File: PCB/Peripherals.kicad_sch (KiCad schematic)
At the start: 25 parts, among them J1 104031-0811, J3 BM04B-GHS-TBT, J4 BM06B-GHS-TBT, J5 BDL-108-X-X, J6 BM06B-GHS-TBT, J7 BM04B-GHS-TBT, U3 FM25V02A-GTR

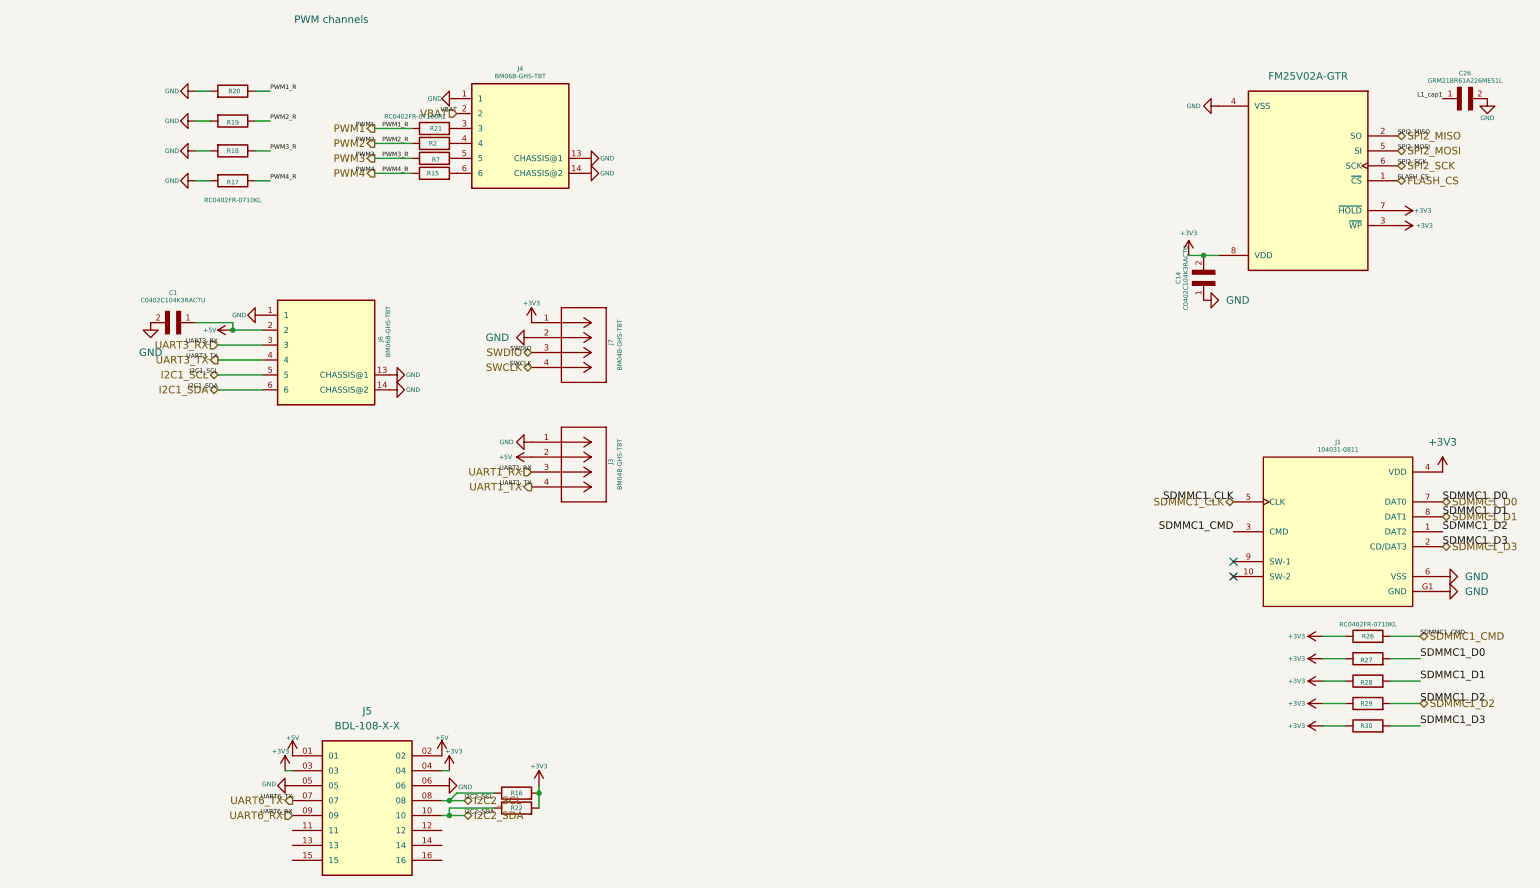
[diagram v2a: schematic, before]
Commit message: Peripherals: replace JST-GH/Samtec with castellated pad-row connectors
- Deleted J3/J4/J5/J6/J7 (JST-GH + Samtec)
- Added J3 GPS(PADROW-6), J4 TELEM(PADROW-5), J5 I2C2(PADROW-4),
  J6 SPI2(PADROW-6), J7 SWD(PADROW-5), J8 GPIO-EXP(HEADER-2x6),
  J9 MOTOR(PADROW-4), J10 BUZZ(PADROW-2), J11 LED(PADROW-2)
- Connected all pads to nets via Konnect connect_to_net
- NOTE: PWM series-resistor network (R2/R7/R15/R21) now orphaned, needs rebuild
- New nets needing root connection: GPIO_A0..A7, BUZZ, LED, NRST
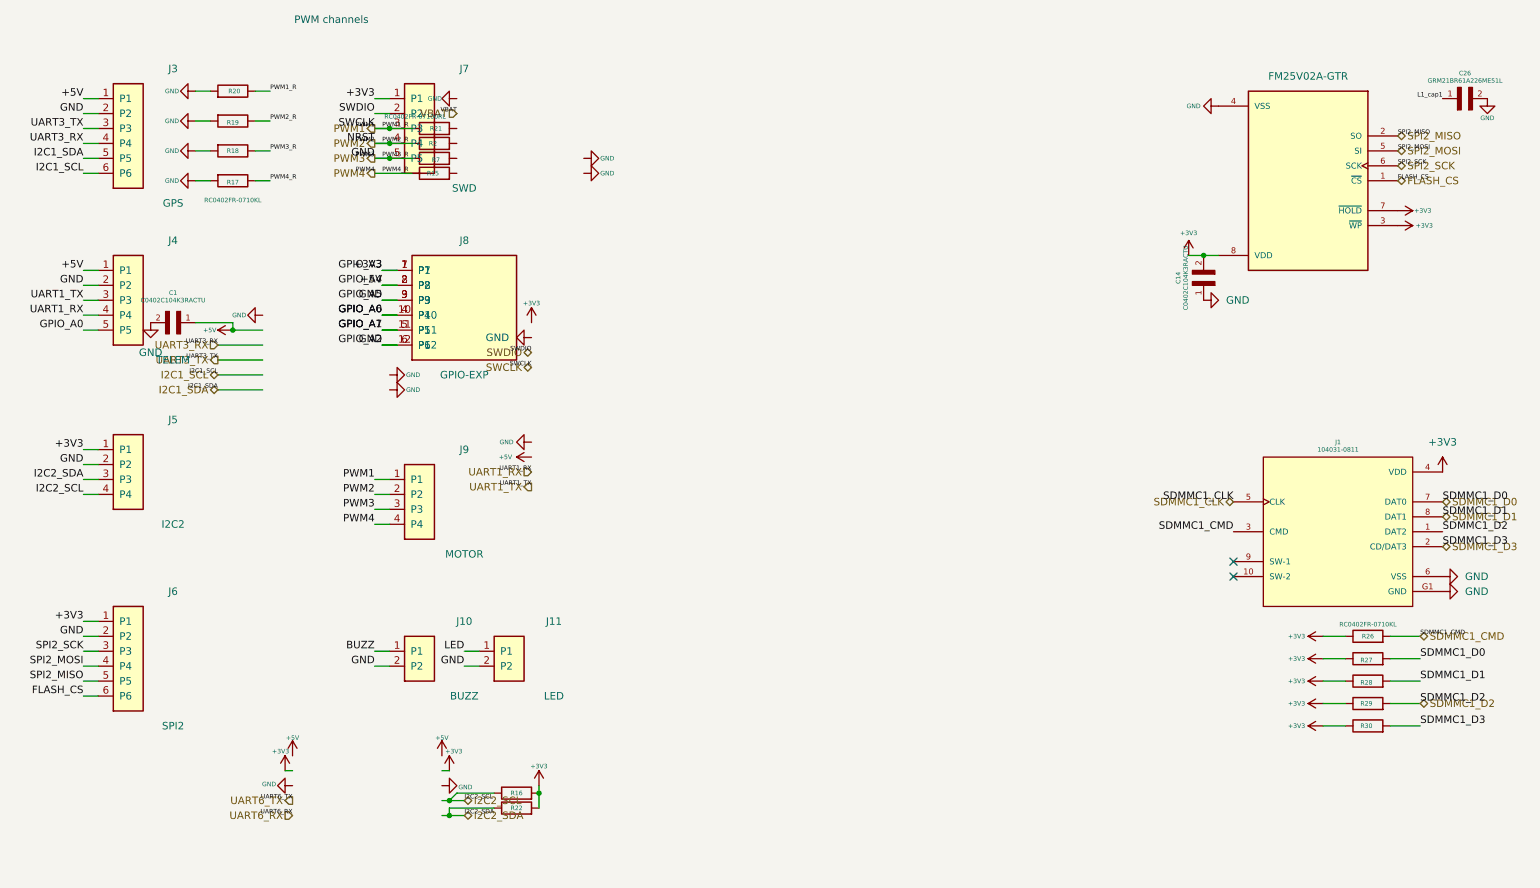
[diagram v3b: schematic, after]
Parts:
- removed J3, J7: BM04B-GHS-TBT, BM04B-GHS-TBT:CONN_BM04B-GHS-TBT_JST, symbol BM04B-GHS-TBT:BM04B-GHS-TBT
- removed J4, J6: BM06B-GHS-TBT, BM06B-GHS-TBT:BM06B-GHS-TBT, symbol BM06B-GHS-TBT:BM06B-GHS-TBT
- removed J5: BDL-108-X-X, BDL-108-X-X:SAMTEC_BDL-108-X-X, symbol BDL-108-X-X:BDL-108-X-X
- added J10: BUZZ, OpenVCU:PADROW-2, symbol OpenVCU:CONN-2
- added J11: LED, OpenVCU:PADROW-2, symbol OpenVCU:CONN-2
- added J3: GPS, OpenVCU:PADROW-6, symbol OpenVCU:CONN-6
- added J4: TELEM, OpenVCU:PADROW-5, symbol OpenVCU:CONN-5
- added J5: I2C2, OpenVCU:PADROW-4, symbol OpenVCU:CONN-4
- added J6: SPI2, OpenVCU:PADROW-6, symbol OpenVCU:CONN-6
- added J7: SWD, OpenVCU:PADROW-5, symbol OpenVCU:CONN-5
- added J8: GPIO-EXP, OpenVCU:HEADER-2x6, symbol OpenVCU:CONN-2x6
- added J9: MOTOR, OpenVCU:PADROW-4, symbol OpenVCU:CONN-4
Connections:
- net PWM3 is gone; now on net GND: R18.1, R7.1
- net +3V3: now also J5.1 (P1), J6.1 (P1), J7.1 (P1), J8.1 (P1), J8.7 (P7)
- net +5V: now also J3.1 (P1), J4.1 (P1), J8.2 (P2), J8.8 (P8)
- net FLASH_CS: now also J6.6 (P6)
- net GND: now also J10.2 (P2), J11.2 (P2), J3.2 (P2), J4.2 (P2), J5.2 (P2), J6.2 (P2), J7.5 (P5), J8.12 (P12), J8.3 (P3), J8.6 (P6), J8.9 (P9), J9.3 (P3)
- net I2C1_SCL: now also J3.6 (P6)
- net I2C1_SDA: now also J3.5 (P5)
- net I2C2_SCL: now also J5.4 (P4)
- net I2C2_SDA: now also J5.3 (P3)
- net PWM1: now also J7.3 (P3), J9.1 (P1)
- net PWM2: now also J7.4 (P4), J9.2 (P2)
- net PWM4: now also J9.4 (P4)
- net SPI2_MISO: now also J6.5 (P5)
- net SPI2_MOSI: now also J6.4 (P4)
- net SPI2_SCK: now also J6.3 (P3)
- net SWDIO: now also J7.2 (P2)
- net UART1_RX: now also J4.4 (P4)
- net UART1_TX: now also J4.3 (P3)
- net UART3_RX: now also J3.4 (P4)
- net UART3_TX: now also J3.3 (P3)
- new net BUZZ: J10.1 (P1)
- new net GPIO_A0: J4.5 (P5), J8.10 (P10), J8.4 (P4)
- new net GPIO_A1: J8.11 (P11), J8.5 (P5)
- new net LED: J11.1 (P1)

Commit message: Peripherals+root: SWD header, GPIO expansion, PWM output stage, LED/BUZZ/BARO_INT
Peripherals (PCB/Peripherals.kicad_sch):
- J7 (CONN-5) is a proper SWD header: +3V3 / SWDIO / SWCLK / NRST / GND,
  first three exported as hierarchical labels matching the existing root sheet pins.
- J8 (CONN-2x6) expansion header: +3V3, +5V, GND, GND, GPIO_A0..GPIO_A7.
  GPIO_A0..A7 are hierarchical labels on new left-edge sheet pins.
- PWM output stage PWMn -> 100R (R21/R2/R7/R15) -> PWMn_R -> J9 (motor header),
  with the existing 10k R20/R19/R18/R17 as pull-downs on PWMn_R.
- J10 BUZZ and J11 LED exported as hierarchical labels; J4.5 spare TELEM pad -> GND.
- Removed 6 duplicate wires, 4 dead SWDIO/SWCLK labels, 2 floating power symbols.

Root (PCB/OpenVCU.kicad_sch):
- GPIO_A0..A7 on U1.1/2/3/37/22/23/24/28, BUZZ on U1.90 (PB4/TIM16_CH1),
  LED on U1.34 (PB0), BARO_INT on U1.88 (PD7/EXTI7); stale SPI_CS_GYRO and
  BMI_INT3 references cleared.
- 20 no_connect markers added on reserved/spare MCU pins.
- 11 new sheet pins + matching labels on the left edge of the Peripherals sheet box,
  plus NRST at (222.25,135.89).

Library (PCB/OpenVCU.kicad_sym):
- CONN-2x6 pads 7..12 moved to x=+11.43 so the 2x6 header has two columns.

ERC: 282 -> 249 (49 errors, 200 warnings).
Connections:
- net +3V3: no longer J8.7 (P7)
- net +5V: no longer J8.8 (P8)
- net GND: now also J4.5 (P5), J8.4 (P4); no longer J8.12 (P12), J8.6 (P6), J8.9 (P9), J9.3 (P3), R18.1, R7.1
- net GPIO_A0: now also J8.5 (P5); no longer J4.5 (P5), J8.10 (P10), J8.4 (P4)
- net GPIO_A1: now also J8.6 (P6); no longer J8.11 (P11), J8.5 (P5)
- net PWM1: no longer J7.3 (P3), J9.1 (P1), R20.1
- net PWM2: no longer J7.4 (P4), J9.2 (P2), R19.1
- net PWM4: no longer J9.4 (P4), R17.1
- net PWM1_R: now reaches R21.2
- net PWM1_R: now also J9.1 (P1), R20.1
- net PWM4_R: now reaches R15.2
- net PWM4_R: now also J9.4 (P4), R17.1
- net PWM3_R: now reaches R7.2
- net PWM3_R: now also J9.3 (P3), R18.1
- net PWM2_R: now reaches R2.2
- net PWM2_R: now also J9.2 (P2), R19.1
- new net GPIO_A2: J8.7 (P7)
- new net GPIO_A3: J8.8 (P8)
- new net GPIO_A4: J8.9 (P9)
- new net GPIO_A5: J8.10 (P10)
- new net GPIO_A6: J8.11 (P11)
- new net GPIO_A7: J8.12 (P12)
- new net NRST: J7.4 (P4)
- new net PWM3: R7.1
- new net SWCLK: J7.3 (P3)

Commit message: Power: fix the shorted buck input rail (VBAT)
The buck input network was silently shorted to GND and had no VBAT net at all:

  * L1.1 (inductor, SW side) was wired to the +5V node instead of SW, shorting
    SW to +5V through the inductor
  * C51.2's GND stub passed straight through R50.1's pin, dragging the TPS54360
    feedback/EN divider top and VIN down to GND

Rebuild the VBAT tap and the +5V output node so that

  /Power/VBAT = C51.1, C52.1, C53.1, R50.1, U9.2 (VIN)
  /Power/SW   = C50.2, D1.1, L1.1, U9.8          (catch diode + inductor)
  +5V         = C55.1, C56.1, L1.2, R53.1, ...

Also drop the vestigial VBAT hierarchical pin (Power + Peripherals) and its two
root labels: nothing on the root or Peripherals sheets consumes battery voltage,
and the MCU VBAT pin is tied to +3V3 on the root, so it was dangling.
Add a PWR_FLAG on the VBAT rail.

New tools: /tmp/opencode/overlap.py and junctions.py detect collinear-overlap and
T-junction shorts, which ERC does not report.

ERC: 0 errors.
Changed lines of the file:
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@@
-		)
-	)
-	(label "VBAT"
-		(at 78.74 33.02 180)
-		(effects
-			(font
-				(size 0.762 0.762)
-			)
-			(justify right bottom)
 		)
 	)
@@
 		(effects
 			(font
-				(size 1.27 1.27)
-			)
-			(justify right)
-		)
-	)
-	(hierarchical_label "VBAT"
-		(shape input)
-		(at 78.74 33.02 180)
-		(effects
-			(font

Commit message: Peripherals: break out UART6, clear stub wires, tie C26 to +3V3
  * add J13 (PADROW-5): UART6_TX / UART6_RX / GND x3, so the two UART6 sheet
    pins now terminate on a real connector instead of dangling mid-sheet
  * delete nine zero-length / dangling wire stubs left over from earlier edits
  * delete #PWR078/#PWR079 (duplicate +3V3 symbols stranded by the stub cleanup)
  * C26 pin1 was labelled L1_cap1 with nothing on the other side; tie it to +3V3

ERC: 0 errors, 201 -> 173 warnings.
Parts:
- added J13: PADROW-5, OpenVCU:PADROW-5, symbol OpenVCU:CONN-5
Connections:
- net GPIO_A0 is gone; now on net GND: J8.5 (P5)
- net L1_cap1 is gone; now on net +3V3: C26.1
- net +3V3: now also J13.1 (P1)
- net +5V: now also J13.2 (P2)
- net GND: now also J13.3 (P3), J13.4 (P4), J13.5 (P5)
